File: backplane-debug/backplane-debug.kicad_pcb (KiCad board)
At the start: 2 copper layers, 41 x 29.5 mm, 3 parts, among them J1 M55-7101642R, J2 Conn_02x08_Odd_Even

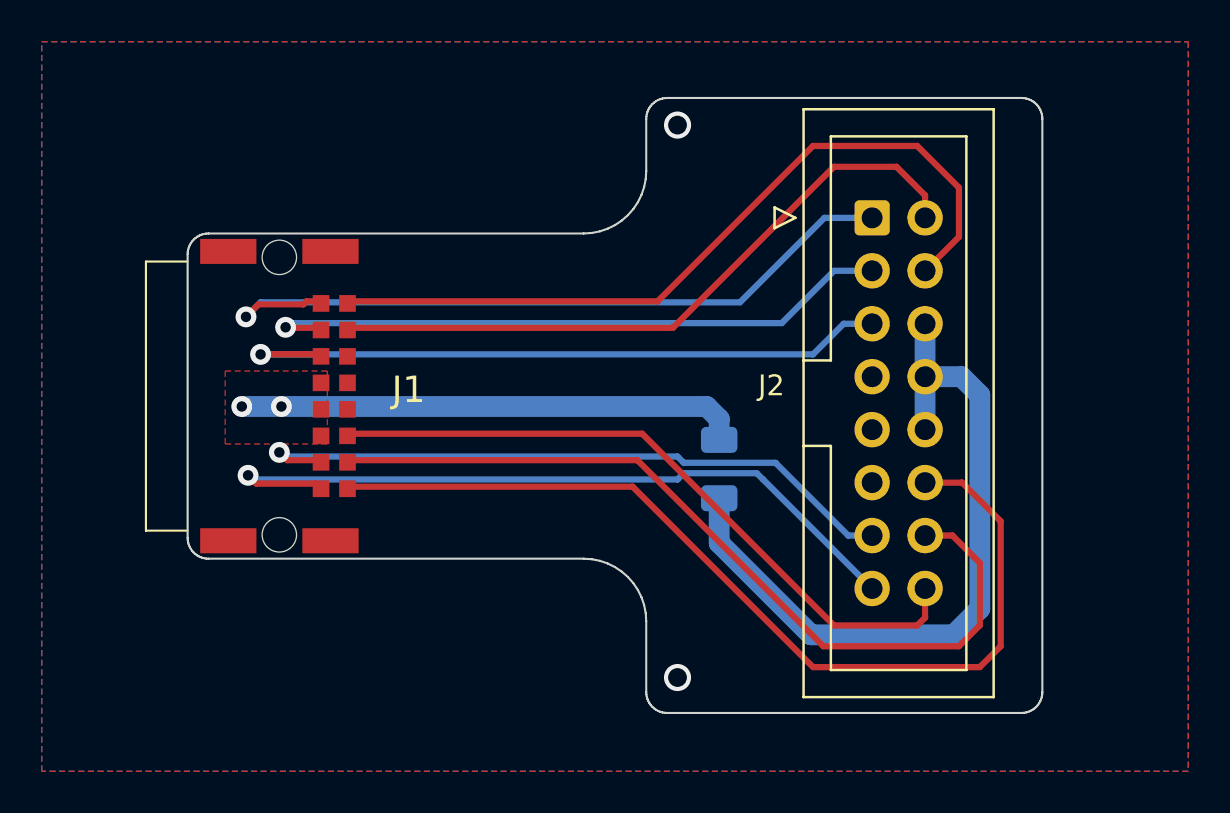
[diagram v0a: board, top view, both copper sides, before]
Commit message: Updated FlatSat breakout and backplane debug board layouts after design review
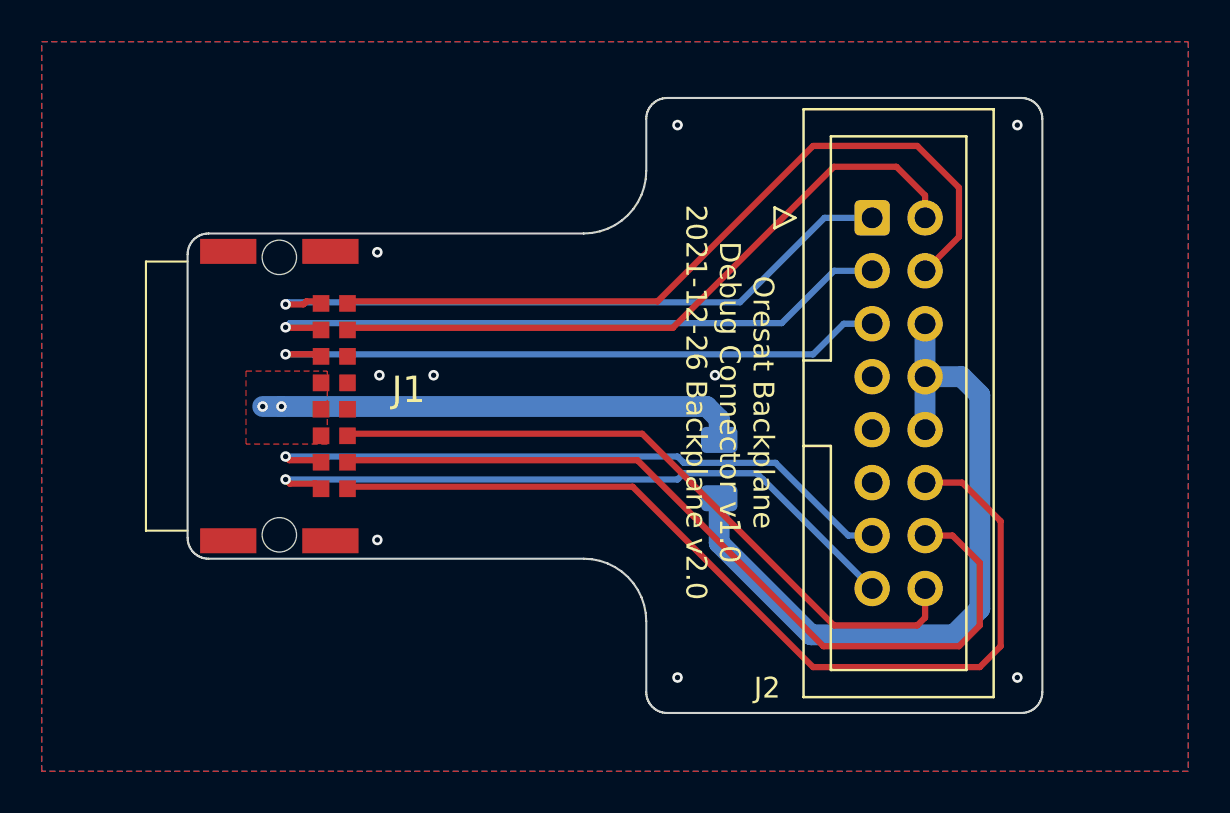
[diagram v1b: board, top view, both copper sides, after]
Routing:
- net SD: track 35.8 -> 31.5 mm
- net OPD_SCL: track 36.1 -> 32.3 mm
- net CAN1_H: track 32.7 -> 30.3 mm
- net Net-(F1-Pad2): track 24.1 -> 23.1 mm
- net CAN2_H: track 32.1 -> 31.4 mm
- net GND: vias 2 -> 9
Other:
- board text added: "Oresat Backplane Debug Connector v1.0 2021-12-26 Backplane v2.0"
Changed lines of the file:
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@@
     (property "Sheetname" "")
     (attr through_hole)
-    (fp_text reference "J2" (at -4.835 8.05) (layer "F.SilkS")
+    (fp_text reference "J2" (at -5.035 22.55) (layer "F.SilkS")
       (effects (font (size 1 1) (thickness 0.15)))
     )
@@
   (gr_poly
     (pts
-      (xy 146 94.8)
+      (arc (start 149 97.8) (mid 148.12132 95.67868) (end 146 94.8))
       (arc (start 128 94.8) (mid 127.292893 94.507107) (end 127 93.8))
       (arc (start 127 80.2) (mid 127.292893 79.492893) (end 128 79.2))
@@
       (arc (start 168 101.2) (mid 167.707107 101.907107) (end 167 102.2))
       (arc (start 150 102.2) (mid 149.292893 101.907107) (end 149 101.2))
-      (arc (start 149 97.8) (mid 148.12132 95.67868) (end 146 94.8))
     ) (layer "Edge.Cuts") (width 0.1) (fill none))
   (gr_poly
@@
       (xy 168 72.7)
     ) (layer "User.4") (width 0.1) (fill none))
+  (gr_text "Oresat Backplane\nDebug Connector v1.0\n2021-12-26 Backplane v2.0" (at 153 87.3 270) (layer "F.SilkS")
+    (effects (font (size 1 1) (thickness 0.15)))
+  )
   (segment (start 165 97.2) (end 165 86.95) (width 1) (layer "B.Cu") (net 1))
   (segment (start 163.75 98.45) (end 165 97.2) (width 1) (layer "B.Cu") (net 1))
@@
   (segment (start 165 86.95) (end 164.12 86.07) (width 1) (layer "B.Cu") (net 1))
   (segment (start 152.5 94.05) (end 156.9 98.45) (width 1) (layer "B.Cu") (net 1))
-  (via (at 129.6 87.5) (size 1) (drill 0.5) (layers "F.Cu" "B.Cu") (free) (net 2))
-  (via (at 131.5 87.5) (size 1) (drill 0.5) (layers "F.Cu" "B.Cu") (net 2))
-  (segment (start 129.6 87.5) (end 151.9 87.5) (width 1) (layer "B.Cu") (net 2))
+  (via (at 131.5 87.5) (size 0.508) (drill 0.254) (layers "F.Cu" "B.Cu") (net 2))
+  (via (at 130.6 87.5) (size 0.508) (drill 0.254) (layers "F.Cu" "B.Cu") (net 2))
+  (segment (start 130.6 87.5) (end 131.5 87.5) (width 1) (layer "B.Cu") (net 2))
+  (segment (start 131.5 87.5) (end 151.9 87.5) (width 1) (layer "B.Cu") (net 2))
   (segment (start 152.5 88.1) (end 152.5 89.1) (width 1) (layer "B.Cu") (net 2))
   (segment (start 151.9 87.5) (end 152.5 88.1) (width 1) (layer "B.Cu") (net 2))
+  (segment (start 131.7 91) (end 131.9 91.2) (width 0.3) (layer "F.Cu") (net 3))
+  (segment (start 131.9 91.2) (end 133.155 91.2) (width 0.3) (layer "F.Cu") (net 3))
   (segment (start 133.155 91.2) (end 133.3 91.345) (width 0.3) (layer "F.Cu") (net 3))
-  (segment (start 130.3 91.2) (end 133.155 91.2) (width 0.3) (layer "F.Cu") (net 3))
-  (segment (start 129.9 90.8) (end 130.3 91.2) (width 0.3) (layer "F.Cu") (net 3))
-  (via (at 129.9 90.8) (size 1) (drill 0.5) (layers "F.Cu" "B.Cu") (net 3))
-  (segment (start 129.9 90.8) (end 130.1 91) (width 0.3) (layer "B.Cu") (net 3))
+  (via (at 131.7 91) (size 0.508) (drill 0.254) (layers "F.Cu" "B.Cu") (net 3))
   (segment (start 154.605 91) (end 159.835 96.23) (width 0.3) (layer "B.Cu") (net 3))
+  (segment (start 154.3 90.7) (end 154.605 91) (width 0.3) (layer "B.Cu") (net 3))
+  (segment (start 131.7 91) (end 150.5 91) (width 0.3) (layer "B.Cu") (net 3))
   (segment (start 150.5 91) (end 150.8 90.7) (width 0.3) (layer "B.Cu") (net 3))
-  (segment (start 130.1 91) (end 150.5 91) (width 0.3) (layer "B.Cu") (net 3))
-  (segment (start 154.3 90.7) (end 154.605 91) (width 0.3) (layer "B.Cu") (net 3))
   (segment (start 150.8 90.7) (end 154.3 90.7) (width 0.3) (layer "B.Cu") (net 3))
-  (segment (start 131.775 90.075) (end 133.3 90.075) (width 0.3) (layer "F.Cu") (net 4))
-  (segment (start 131.4 89.7) (end 131.775 90.075) (width 0.3) (layer "F.Cu") (net 4))
-  (via (at 131.4 89.7) (size 1) (drill 0.5) (layers "F.Cu" "B.Cu") (net 4))
-  (segment (start 131.4 89.7) (end 131.6 89.9) (width 0.3) (layer "B.Cu") (net 4))
+  (segment (start 131.875 90.075) (end 133.3 90.075) (width 0.3) (layer "F.Cu") (net 4))
+  (segment (start 131.7 89.9) (end 131.875 90.075) (width 0.3) (layer "F.Cu") (net 4))
+  (via (at 131.7 89.9) (size 0.508) (drill 0.254) (layers "F.Cu" "B.Cu") (net 4))
+  (segment (start 150.8 90.2) (end 155.2 90.2) (width 0.3) (layer "B.Cu") (net 4))
   (segment (start 158.69 93.69) (end 159.835 93.69) (width 0.3) (layer "B.Cu") (net 4))
+  (segment (start 131.7 89.9) (end 150.5 89.9) (width 0.3) (layer "B.Cu") (net 4))
+  (segment (start 155.2 90.2) (end 158.69 93.69) (width 0.3) (layer "B.Cu") (net 4))
   (segment (start 150.5 89.9) (end 150.8 90.2) (width 0.3) (layer "B.Cu") (net 4))
-  (segment (start 155.2 90.2) (end 158.69 93.69) (width 0.3) (layer "B.Cu") (net 4))
-  (segment (start 131.6 89.9) (end 150.5 89.9) (width 0.3) (layer "B.Cu") (net 4))
-  (segment (start 150.8 90.2) (end 155.2 90.2) (width 0.3) (layer "B.Cu") (net 4))
-  (segment (start 130.505 84.995) (end 133.3 84.995) (width 0.3) (layer "F.Cu") (net 5))
-  (segment (start 130.5 85) (end 130.505 84.995) (width 0.3) (layer "F.Cu") (net 5))
-  (via (at 130.5 85) (size 1) (drill 0.5) (layers "F.Cu" "B.Cu") (net 5))
+  (segment (start 131.7 84.995) (end 133.3 84.995) (width 0.3) (layer "F.Cu") (net 5))
+  (via (at 131.7 84.995) (size 0.508) (drill 0.254) (layers "F.Cu" "B.Cu") (net 5))
+  (segment (start 157 85) (end 158.47 83.53) (width 0.3) (layer "B.Cu") (net 5))
   (segment (start 158.47 83.53) (end 159.835 83.53) (width 0.3) (layer "B.Cu") (net 5))
-  (segment (start 157 85) (end 158.47 83.53) (width 0.3) (layer "B.Cu") (net 5))
-  (segment (start 130.5 85) (end 157 85) (width 0.3) (layer "B.Cu") (net 5))
+  (segment (start 131.7 84.995) (end 131.705 85) (width 0.3) (layer "B.Cu") (net 5))
+  (segment (start 131.705 85) (end 157 85) (width 0.3) (layer "B.Cu") (net 5))
   (segment (start 131.7 83.7) (end 131.725 83.725) (width 0.3) (layer "F.Cu") (net 6))
   (segment (start 131.725 83.725) (end 133.3 83.725) (width 0.3) (layer "F.Cu") (net 6))
-  (via (at 131.7 83.7) (size 1) (drill 0.5) (layers "F.Cu" "B.Cu") (net 6))
+  (via (at 131.7 83.7) (size 0.508) (drill 0.254) (layers "F.Cu" "B.Cu") (net 6))
   (segment (start 131.9 83.5) (end 155.5 83.5) (width 0.3) (layer "B.Cu") (net 6))
   (segment (start 158.01 80.99) (end 159.835 80.99) (width 0.3) (layer "B.Cu") (net 6))
   (segment (start 131.7 83.7) (end 131.9 83.5) (width 0.3) (layer "B.Cu") (net 6))
   (segment (start 155.5 83.5) (end 158.01 80.99) (width 0.3) (layer "B.Cu") (net 6))
+  (segment (start 132.555 82.6) (end 132.7 82.455) (width 0.3) (layer "F.Cu") (net 7))
+  (segment (start 131.7 82.6) (end 132.555 82.6) (width 0.3) (layer "F.Cu") (net 7))
   (segment (start 132.7 82.455) (end 133.3 82.455) (width 0.3) (layer "F.Cu") (net 7))
-  (segment (start 129.8 83.2) (end 130.4 82.6) (width 0.3) (layer "F.Cu") (net 7))
-  (segment (start 132.555 82.6) (end 132.7 82.455) (width 0.3) (layer "F.Cu") (net 7))
-  (segment (start 130.4 82.6) (end 132.555 82.6) (width 0.3) (layer "F.Cu") (net 7))
-  (via (at 129.8 83.2) (size 1) (drill 0.5) (layers "F.Cu" "B.Cu") (net 7))
-  (segment (start 130.5 82.5) (end 153.5 82.5) (width 0.3) (layer "B.Cu") (net 7))
+  (via (at 131.7 82.6) (size 0.508) (drill 0.254) (layers "F.Cu" "B.Cu") (net 7))
+  (segment (start 131.7 82.6) (end 131.8 82.5) (width 0.3) (layer "B.Cu") (net 7))
+  (segment (start 131.8 82.5) (end 153.5 82.5) (width 0.3) (layer "B.Cu") (net 7))
+  (segment (start 157.55 78.45) (end 159.835 78.45) (width 0.3) (layer "B.Cu") (net 7))
   (segment (start 153.5 82.5) (end 157.55 78.45) (width 0.3) (layer "B.Cu") (net 7))
-  (segment (start 129.8 83.2) (end 130.5 82.5) (width 0.3) (layer "B.Cu") (net 7))
-  (segment (start 157.55 78.45) (end 159.835 78.45) (width 0.3) (layer "B.Cu") (net 7))
   (segment (start 157 100) (end 165 100) (width 0.3) (layer "F.Cu") (net 8))
   (segment (start 165 100) (end 166 99) (width 0.3) (layer "F.Cu") (net 8))
@@
   (segment (start 134.57 88.805) (end 148.805 88.805) (width 0.3) (layer "F.Cu") (net 10))
   (segment (start 162 98) (end 162.375 97.625) (width 0.3) (layer "F.Cu") (net 10))
-  (via (at 150.5 100.5) (size 1.3) (drill 0.9) (layers "F.Cu" "B.Cu") (free) (net 11))
-  (via (at 150.5 74) (size 1.3) (drill 0.9) (layers "F.Cu" "B.Cu") (free) (net 11))
+  (via (at 136.1 93.9) (size 0.508) (drill 0.254) (layers "F.Cu" "B.Cu") (free) (net 11))
+  (via (at 136.1 80.1) (size 0.508) (drill 0.254) (layers "F.Cu" "B.Cu") (free) (net 11))
+  (via (at 150.5 74) (size 0.508) (drill 0.254) (layers "F.Cu" "B.Cu") (free) (net 11))
+  (via (at 136.2 86) (size 0.508) (drill 0.254) (layers "F.Cu" "B.Cu") (free) (net 11))
+  (via (at 138.8 86) (size 0.508) (drill 0.254) (layers "F.Cu" "B.Cu") (free) (net 11))
+  (via (at 166.8 100.5) (size 0.508) (drill 0.254) (layers "F.Cu" "B.Cu") (free) (net 11))
+  (via (at 166.8 74) (size 0.508) (drill 0.254) (layers "F.Cu" "B.Cu") (free) (net 11))
+  (via (at 150.5 100.5) (size 0.508) (drill 0.254) (layers "F.Cu" "B.Cu") (free) (net 11))
+  (via (at 152.3 86) (size 0.508) (drill 0.254) (layers "F.Cu" "B.Cu") (free) (net 11))
   (segment (start 158 76) (end 161 76) (width 0.3) (layer "F.Cu") (net 12))
   (segment (start 162.375 77.375) (end 162.375 78.45) (width 0.3) (layer "F.Cu") (net 12))
@@
   (segment (start 134.57 82.455) (end 149.545 82.455) (width 0.3) (layer "F.Cu") (net 13))
   (zone (net 11) (net_name "GND") (layer "F.Cu") (hatch edge 0.508)
-    (connect_pads (clearance 0.508))
-    (min_thickness 0.254) (filled_areas_thickness no)
+    (connect_pads (clearance 0.2))
+    (min_thickness 0.2) (filled_areas_thickness no)
     (fill yes (thermal_gap 0.508) (thermal_bridge_width 0.508))
     (polygon
@@
       (pts
         (xy 133.7 89.3)
-        (xy 128.8 89.3)
-        (xy 128.8 85.8)
+        (xy 129.8 89.3)
+        (xy 129.8 85.8)
         (xy 133.7 85.8)
       )
@@
   )
   (zone (net 11) (net_name "GND") (layer "B.Cu") (hatch edge 0.508)
-    (connect_pads (clearance 0.508))
-    (min_thickness 0.254) (filled_areas_thickness no)
+    (connect_pads (clearance 0.2))
+    (min_thickness 0.2) (filled_areas_thickness no)
     (fill yes (thermal_gap 0.508) (thermal_bridge_width 0.508))
     (polygon
